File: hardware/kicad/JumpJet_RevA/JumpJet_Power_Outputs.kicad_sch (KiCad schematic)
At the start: 29 parts, among them J1 24V IN / 20A MIN, J2 PTC 24V / 200W, J3 24V BLOWER, J4 AUX1 DNP, Q1 60V NFET TBD, Q2 60V NFET TBD, Q3 60V NFET DNP, U1 74AHCT125

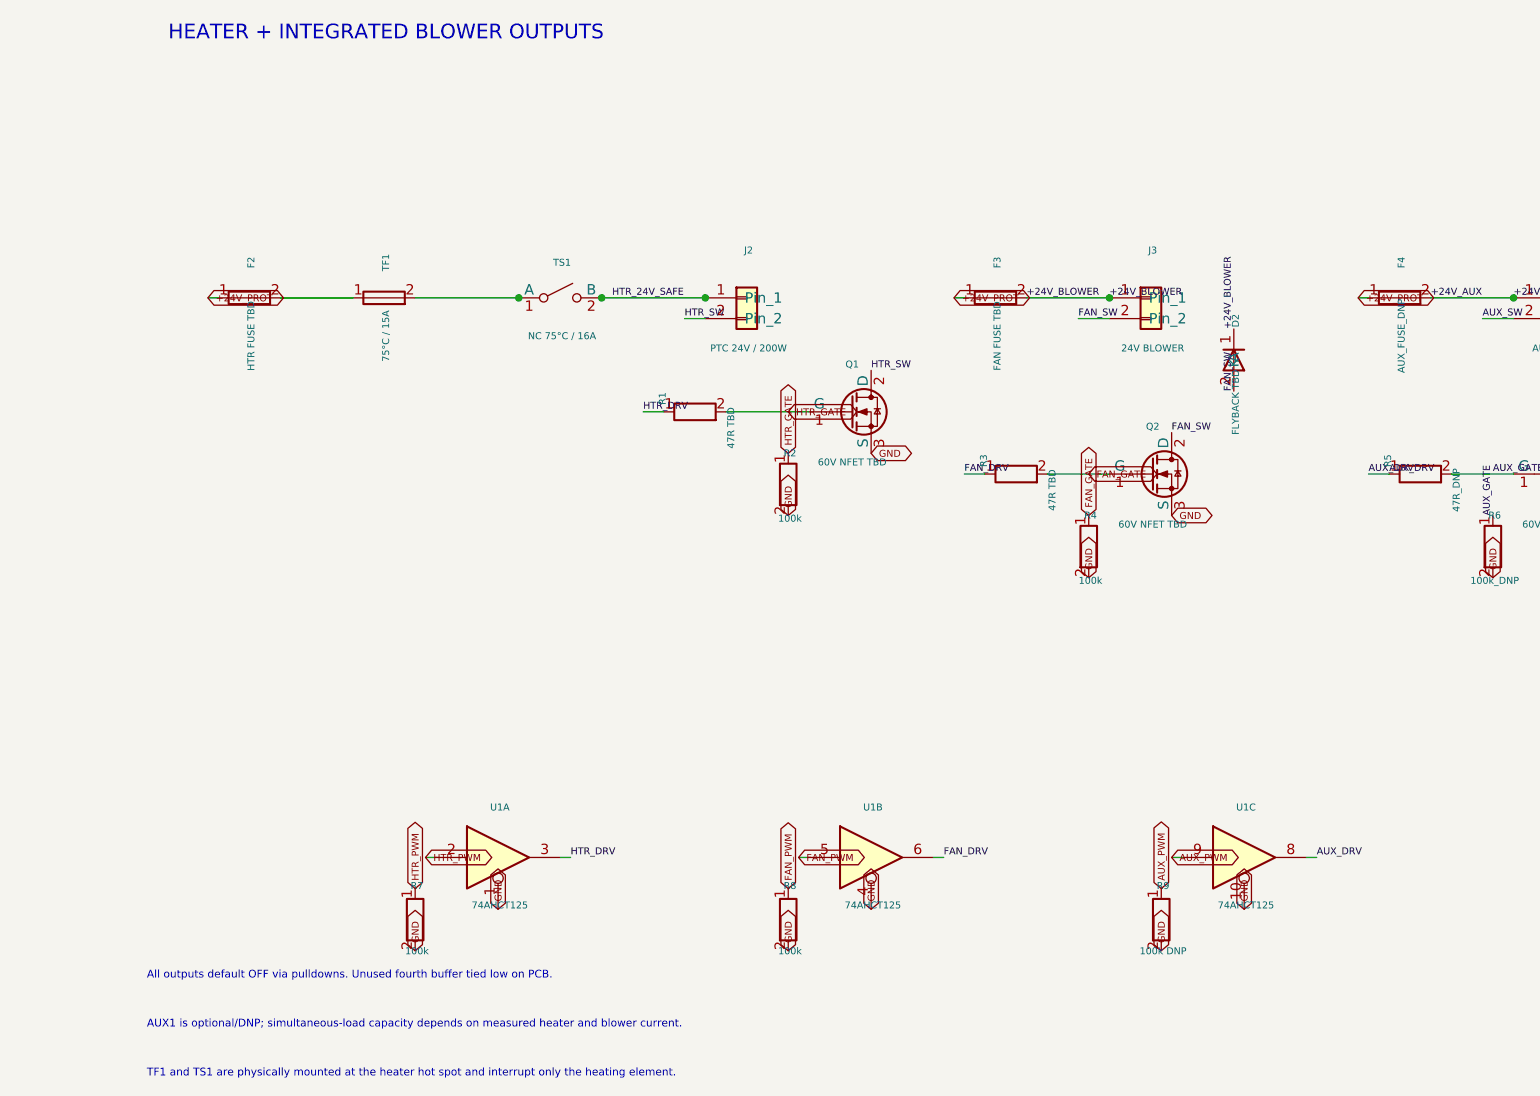
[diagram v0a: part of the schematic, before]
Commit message: hardware: replace fan block with four-wire interface
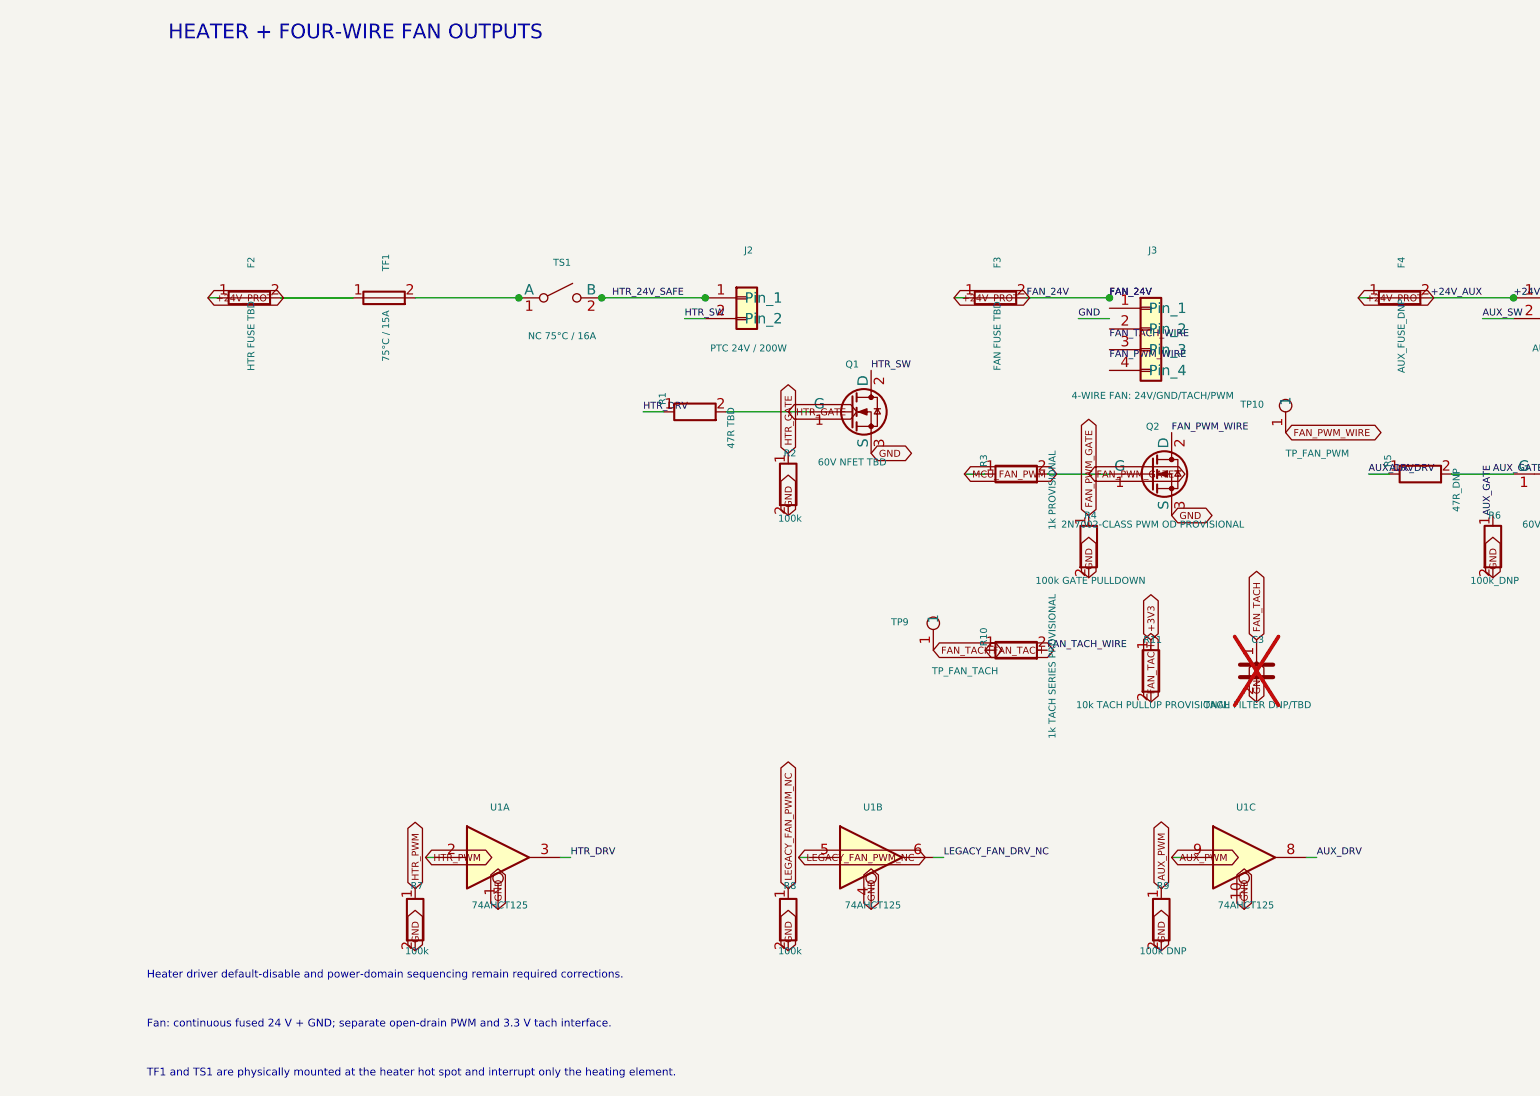
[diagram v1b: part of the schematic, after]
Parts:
- removed D2: FLYBACK TBD, Diode_SMD:D_SMA, symbol Device:D
- added C3: TACH FILTER DNP/TBD, Capacitor_SMD:C_0603_1608Metric, symbol Device:C
- added R10: 1k TACH SERIES PROVISIONAL, Resistor_SMD:R_0603_1608Metric, symbol Device:R
- added R11: 10k TACH PULLUP PROVISIONAL, Resistor_SMD:R_0603_1608Metric, symbol Device:R
- added TP10: TP_FAN_PWM, TestPoint:TestPoint_Pad_D1.5mm, symbol Connector:TestPoint
- added TP9: TP_FAN_TACH, TestPoint:TestPoint_Pad_D1.5mm, symbol Connector:TestPoint
- J3: value 24V BLOWER -> 4-WIRE FAN: 24V/GND/TACH/PWM; footprint Connector_JST:JST_XH_B2B-XH-A_1x02_P2.50mm_Vertical -> Connector_JST:JST_XH_B4B-XH-A_1x04_P2.50mm_Vertical; symbol Connector_Generic:Conn_01x02 -> Connector_Generic:Conn_01x04
- Q2: value 60V NFET TBD -> 2N7002-CLASS PWM OD PROVISIONAL; footprint Package_DirectFET:TBD -> Package_TO_SOT_SMD:SOT-23
- R3: value 47R TBD -> 1k PROVISIONAL
- R4: value 100k -> 100k GATE PULLDOWN
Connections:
- net GND: now also C3.2
- net +24V_BLOWER: no longer names the net of J3.1 (Pin_1)
- net +24V_BLOWER: no longer F3.2
- net FAN_DRV renamed LEGACY_FAN_DRV_NC
- net LEGACY_FAN_DRV_NC: no longer R3.1
- net FAN_GATE renamed FAN_PWM_GATE
- net FAN_PWM renamed LEGACY_FAN_PWM_NC
- net FAN_SW: no longer names the net of J3.2 (Pin_2)
- net FAN_SW: no longer Q2.2 (D)
- new net +3V3: R11.1
- new net FAN_24V: F3.2
- new net FAN_PWM_WIRE: Q2.2 (D), TP10.1
- new net FAN_TACH: C3.1, R10.1, R11.2, TP9.1
- new net FAN_TACH_WIRE: R10.2
- new net MCU_FAN_PWM: R3.1
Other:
- note added: "Fan: continuous fused 24 V + GND; separate open-drain PWM and 3.3 V tach interface."
- note added: "HEATER + FOUR-WIRE FAN OUTPUTS"
- note added: "Heater driver default-disable and power-domain sequencing remain required corrections."
- note removed: "AUX1 is optional/DNP; simultaneous-load capacity depends on measured heater and blower current."
- note removed: "All outputs default OFF via pulldowns. Unused fourth buffer tied low on PCB."
- note removed: "HEATER + INTEGRATED BLOWER OUTPUTS"

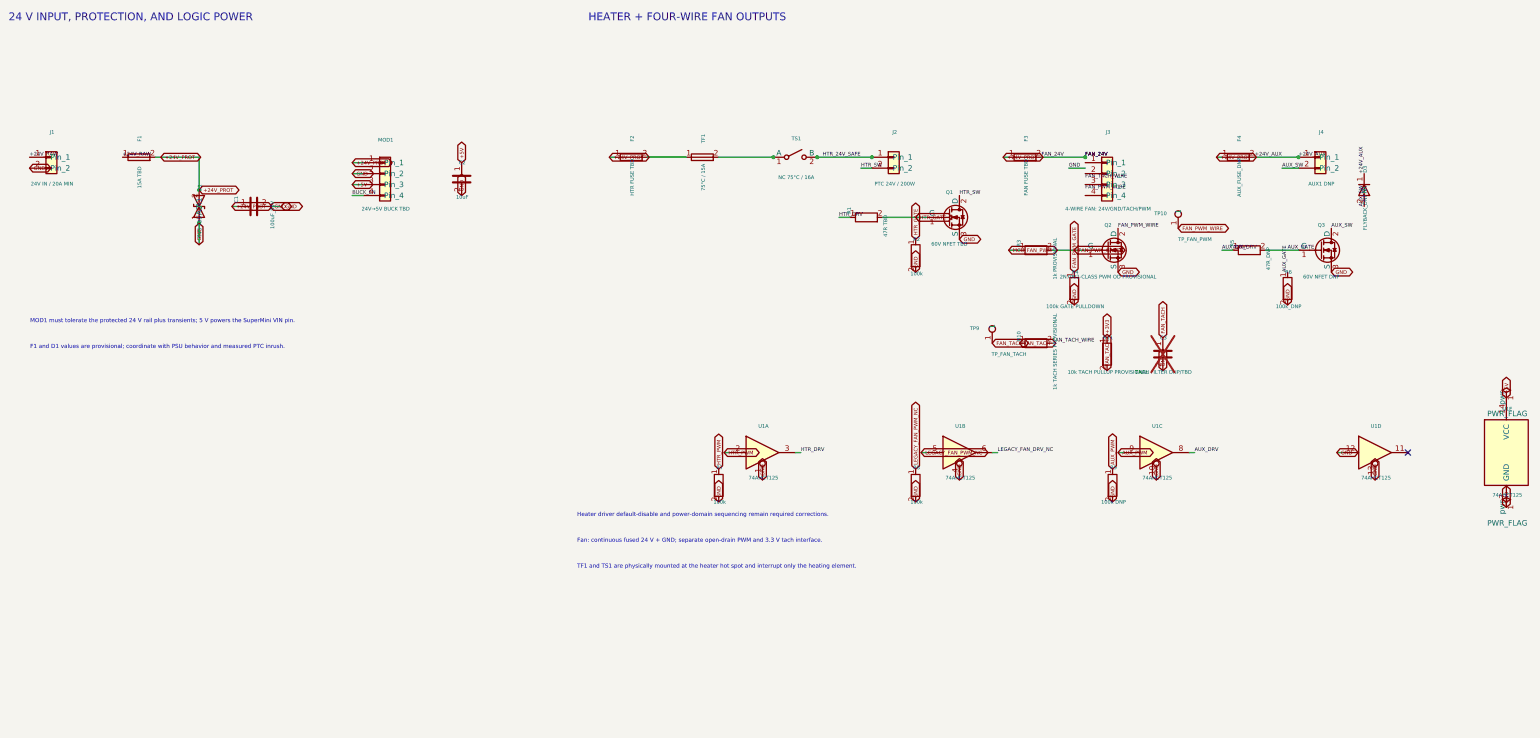
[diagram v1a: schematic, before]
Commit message: hardware: separate gate power and default-disable heater driver
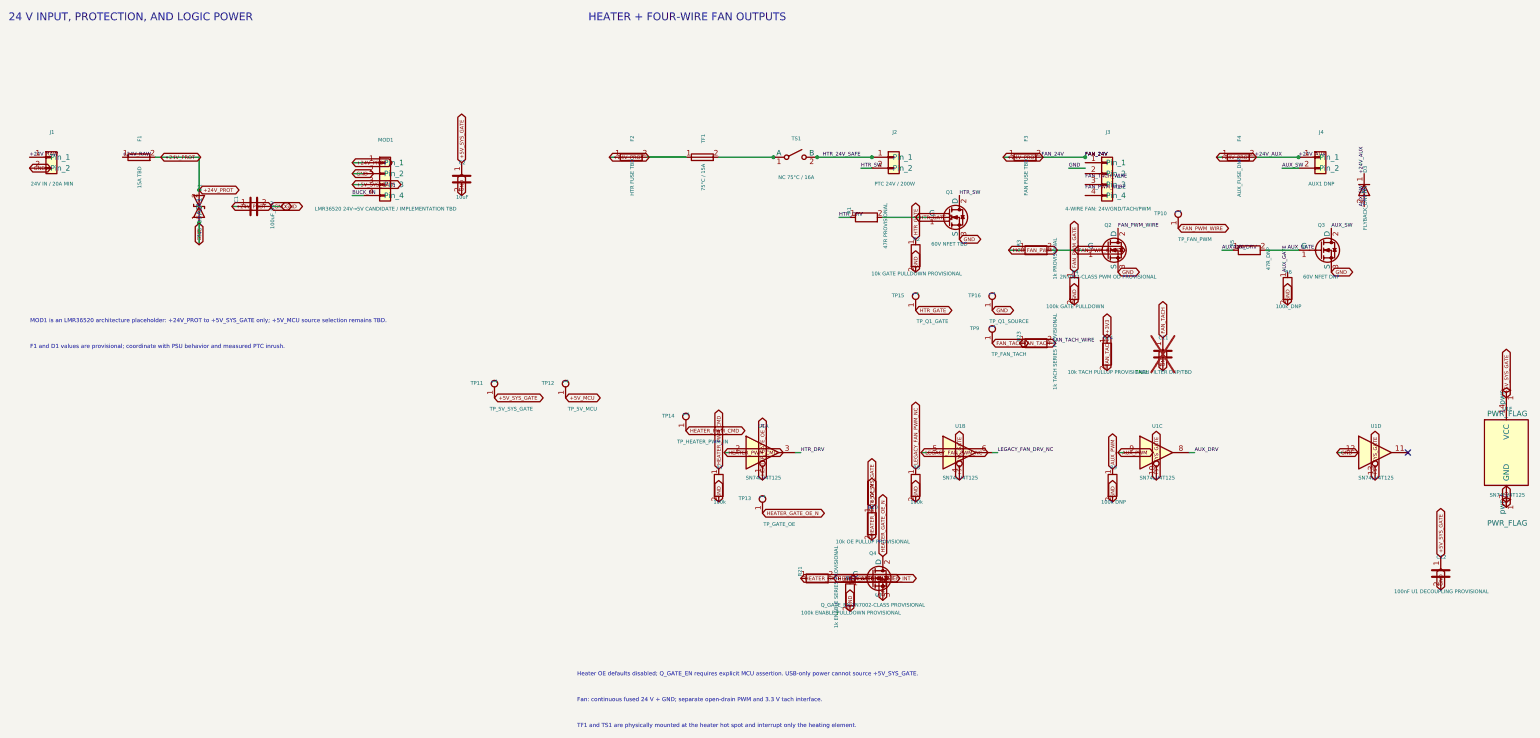
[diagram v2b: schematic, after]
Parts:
- added C12: 100nF U1 DECOUPLING PROVISIONAL, Capacitor_SMD:C_0603_1608Metric, symbol Device:C
- added Q4: Q_GATE_EN 2N7002-CLASS PROVISIONAL, Package_TO_SOT_SMD:SOT-23, symbol Transistor_FET:Q_NMOS_GDS
- added R20: 10k OE PULLUP PROVISIONAL, Resistor_SMD:R_0603_1608Metric, symbol Device:R
- added R21: 1k ENABLE SERIES PROVISIONAL, Resistor_SMD:R_0603_1608Metric, symbol Device:R
- added R22: 100k ENABLE PULLDOWN PROVISIONAL, Resistor_SMD:R_0603_1608Metric, symbol Device:R
- added TP11: TP_5V_SYS_GATE, TestPoint:TestPoint_Pad_D1.5mm, symbol Connector:TestPoint
- added TP12: TP_5V_MCU, TestPoint:TestPoint_Pad_D1.5mm, symbol Connector:TestPoint
- added TP13: TP_GATE_OE, TestPoint:TestPoint_Pad_D1.5mm, symbol Connector:TestPoint
- added TP14: TP_HEATER_PWM_IN, TestPoint:TestPoint_Pad_D1.5mm, symbol Connector:TestPoint
- added TP15: TP_Q1_GATE, TestPoint:TestPoint_Pad_D1.5mm, symbol Connector:TestPoint
- added TP16: TP_Q1_SOURCE, TestPoint:TestPoint_Pad_D1.5mm, symbol Connector:TestPoint
- MOD1: value 24V→5V BUCK TBD -> LMR36520 24V→5V CANDIDATE / IMPLEMENTATION TBD
- R1: value 47R TBD -> 47R PROVISIONAL
- R2: value 100k -> 10k GATE PULLDOWN PROVISIONAL
- U1: value 74AHCT125 -> SN74LV4T125; symbol 74xx:74AHCT125 -> 74xx:SN74LV4T125
- renumbered C3 to C11, R10 to R23, R11 to R24
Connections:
- net GND: now also C12.2, Q4.3 (S), R22.2, TP16.1; no longer U1.1, U1.10, U1.13, U1.4
- net HTR_GATE: now also TP15.1
- net +5V renamed +5V_SYS_GATE
- net +5V_SYS_GATE: now also U1.10, U1.13, U1.4, C12.1, R20.1, TP11.1
- net HTR_PWM renamed HEATER_PWM_CMD
- net HEATER_PWM_CMD: now also TP14.1
- new net +5V_MCU: TP12.1
- new net HEATER_GATE_EN: R21.1
- new net HEATER_GATE_EN_INT: Q4.1 (G), R21.2, R22.1
- new net HEATER_GATE_OE_N: Q4.2 (D), R20.2, TP13.1, U1.1
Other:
- note added: "Heater OE defaults disabled; Q_GATE_EN requires explicit MCU assertion. USB-only power cannot source +5V_SYS_GATE."
- note added: "MOD1 is an LMR36520 architecture placeholder: +24V_PROT to +5V_SYS_GATE only; +5V_MCU source selection remains TBD."
- note removed: "Heater driver default-disable and power-domain sequencing remain required corrections."
- note removed: "MOD1 must tolerate the protected 24 V rail plus transients; 5 V powers the SuperMini VIN pin."

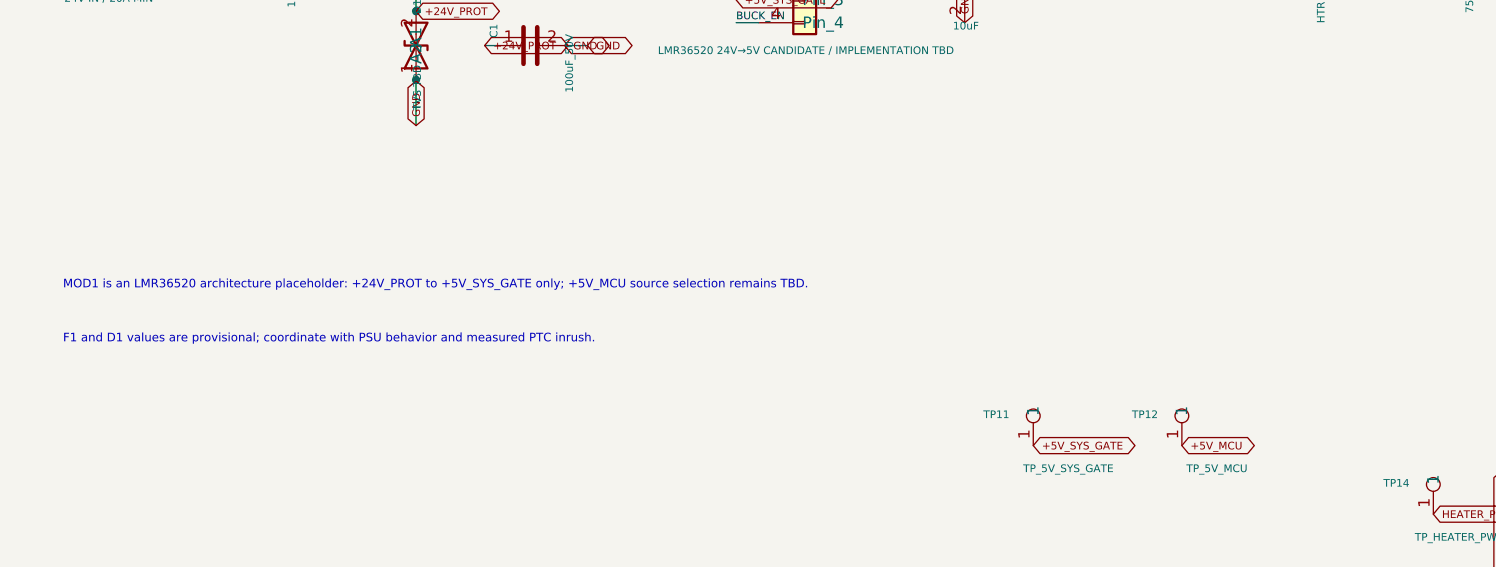
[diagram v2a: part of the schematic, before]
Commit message: hardware: require physical MCU service disconnect
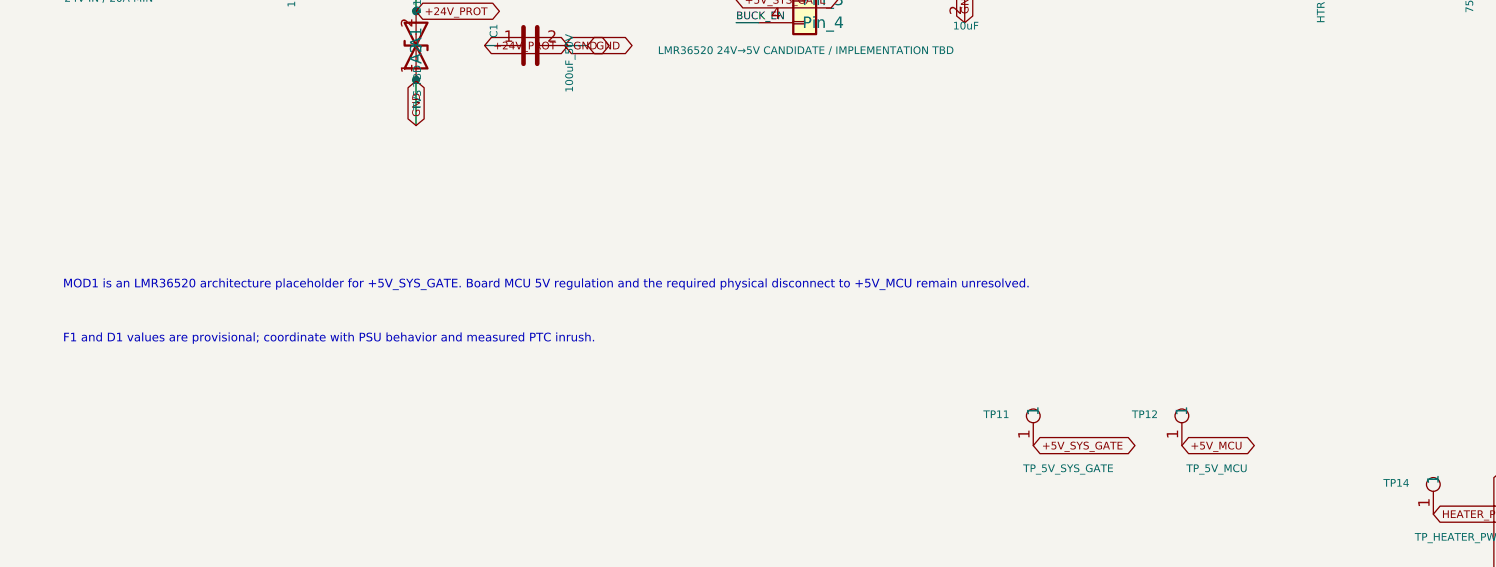
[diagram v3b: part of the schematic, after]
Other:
- note added: "MOD1 is an LMR36520 architecture placeholder for +5V_SYS_GATE. Board MCU 5V regulation and the required physical disconnect to +5V_MCU remain unresolved."
- note removed: "MOD1 is an LMR36520 architecture placeholder: +24V_PROT to +5V_SYS_GATE only; +5V_MCU source selection remains TBD."
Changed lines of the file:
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@@
     (effects (font (size 1.80 1.80) (thickness 0.225)) (justify left bottom))
   )
-  (text "MOD1 is an LMR36520 architecture placeholder: +24V_PROT to +5V_SYS_GATE only; +5V_MCU source selection remains TBD."
+  (text "MOD1 is an LMR36520 architecture placeholder for +5V_SYS_GATE. Board MCU 5V regulation and the required physical disconnect to +5V_MCU remain unresolved."
     (at 23.00 92.00 0)
     (effects (font (size 0.95 0.95) (thickness 0.120)) (justify left bottom))
@@
     (property "Footprint" "TestPoint:TestPoint_Pad_D1.5mm" (at 147.22 108.77 0) (effects (font (size 0.85 0.85)) hide))
     (property "Datasheet" "" (at 147.22 108.77 0) (effects (font (size 0.85 0.85)) hide))
-    (property "Description" "MCU-domain rail test point; source selection remains TBD" (at 147.22 108.77 0) (effects (font (size 0.85 0.85)) hide))
+    (property "Description" "Super Mini-side 5V/USB-VBUS tied-node test point; physical board-5V disconnect is required upstream" (at 147.22 108.77 0) (effects (font (size 0.85 0.85)) hide))
     (pin "1")
     (instances (project "JumpJet_Controller_RevA4" (path "/7daa19f2-c821-405d-9b33-9c66dc62ede9" (reference "TP12") (unit 1))))
